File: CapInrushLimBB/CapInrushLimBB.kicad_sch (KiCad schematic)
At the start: 31 parts, among them J1 Screw_Terminal_01x02, J2 Screw_Terminal_01x02, K1 G5LE-1A, Q1 MPSA42, Q2 IRF9540N, Q3 TIP41C, Q4 BSP230 300V 0.21A, U1 LM385Z-ADJ

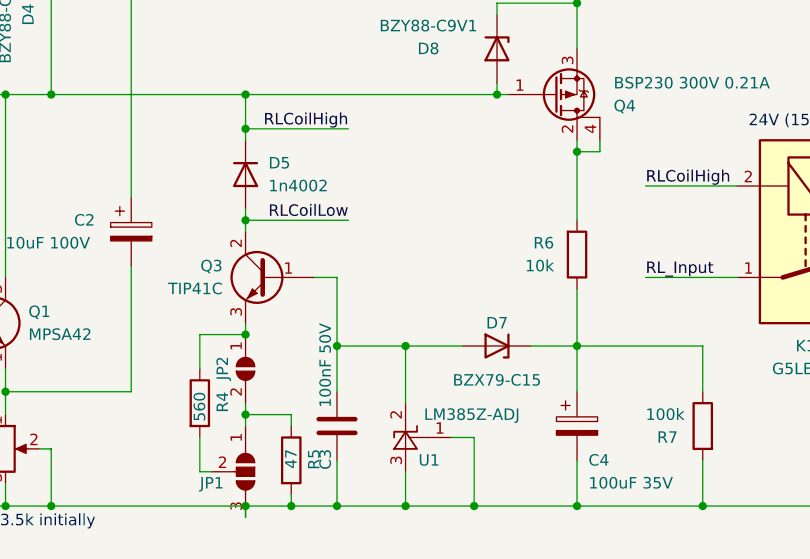
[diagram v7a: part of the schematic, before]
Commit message: Updating model, schematic and PCB to remove cap. on the relay timer ref. and to fit a zener across the relay coil.
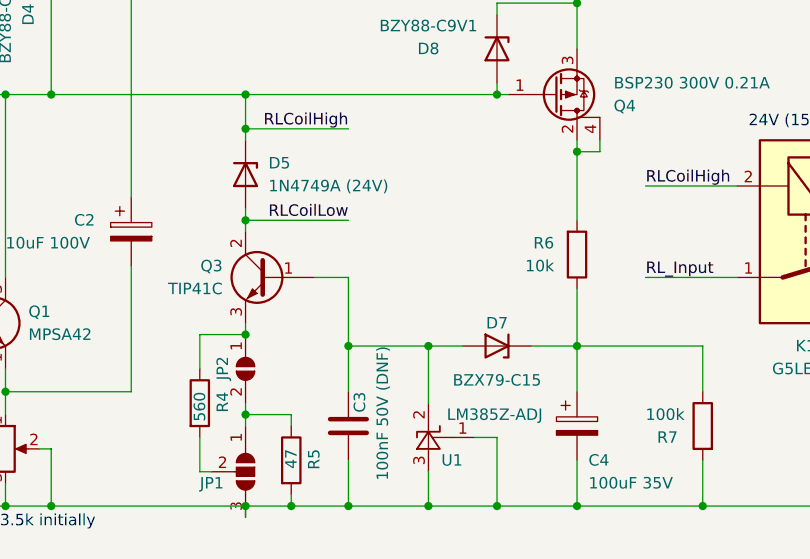
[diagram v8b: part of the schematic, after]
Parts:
- removed D5: 1n4002, Diode_THT:D_DO-41_SOD81_P2.54mm_Vertical_KathodeUp, symbol Device:D
- added D5: 1N4749A (24V), Diode_THT:D_DO-41_SOD81_P2.54mm_Vertical_KathodeUp, symbol Device:D_Zener
- C3: value 100nF 50V -> 100nF 50V (DNF)
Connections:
- net RLCoilHigh: now also D5.1 (K)
- net RLCoilLow: now also D5.2 (A)
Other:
- moved on the sheet: C3, U1
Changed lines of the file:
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@@
   (junction (at 196.85 116.84) (diameter 0) (color 0 0 0 0)
   )
-  (junction (at 142.24 139.7) (diameter 0) (color 0 0 0 0)
-  )
   (junction (at 124.46 97.79) (diameter 0) (color 0 0 0 0)
   )
   (junction (at 102.87 139.7) (diameter 0) (color 0 0 0 0)
   )
+  (junction (at 135.89 139.7) (diameter 0) (color 0 0 0 0)
+  )
   (junction (at 97.79 139.7) (diameter 0) (color 0 0 0 0)
   )
@@
   (junction (at 68.58 139.7) (diameter 0) (color 0 0 0 0)
   )
-  (junction (at 142.24 121.92) (diameter 0) (color 0 0 0 0)
-  )
   (junction (at 124.46 120.65) (diameter 0) (color 0 0 0 0)
   )
@@
   (junction (at 124.46 129.54) (diameter 0) (color 0 0 0 0)
   )
-  (junction (at 134.62 139.7) (diameter 0) (color 0 0 0 0)
-  )
-  (junction (at 149.86 139.7) (diameter 0) (color 0 0 0 0)
+  (junction (at 135.89 121.92) (diameter 0) (color 0 0 0 0)
+  )
+  (junction (at 144.78 139.7) (diameter 0) (color 0 0 0 0)
   )
   (junction (at 111.76 73.66) (diameter 0) (color 0 0 0 0)
   )
+  (junction (at 152.4 139.7) (diameter 0) (color 0 0 0 0)
+  )
   (junction (at 175.26 139.7) (diameter 0) (color 0 0 0 0)
   )
+  (junction (at 144.78 121.92) (diameter 0) (color 0 0 0 0)
+  )
   (junction (at 129.54 139.7) (diameter 0) (color 0 0 0 0)
   )
@@
   (junction (at 97.79 93.98) (diameter 0) (color 0 0 0 0)
   )
-  (junction (at 134.62 121.92) (diameter 0) (color 0 0 0 0)
-  )
   (junction (at 93.98 73.66) (diameter 0) (color 0 0 0 0)
   )
@@
     (stroke (width 0) (type default) (color 0 0 0 0))
   )
-  (wire (pts (xy 149.86 139.7) (xy 161.29 139.7))
+  (wire (pts (xy 144.78 139.7) (xy 152.4 139.7))
     (stroke (width 0) (type default) (color 0 0 0 0))
   )
@@
     (stroke (width 0) (type default) (color 0 0 0 0))
   )
-  (wire (pts (xy 132.08 114.3) (xy 134.62 114.3))
+  (wire (pts (xy 132.08 114.3) (xy 135.89 114.3))
     (stroke (width 0) (type default) (color 0 0 0 0))
   )
@@
     (stroke (width 0) (type default) (color 0 0 0 0))
   )
-  (wire (pts (xy 149.86 132.08) (xy 149.86 139.7))
+  (wire (pts (xy 152.4 132.08) (xy 152.4 139.7))
     (stroke (width 0) (type default) (color 0 0 0 0))
   )
@@
     (stroke (width 0) (type default) (color 0 0 0 0))
   )
-  (wire (pts (xy 134.62 139.7) (xy 142.24 139.7))
-    (stroke (width 0) (type default) (color 0 0 0 0))
-  )
-  (wire (pts (xy 142.24 121.92) (xy 148.59 121.92))
-    (stroke (width 0) (type default) (color 0 0 0 0))
-  )
   (wire (pts (xy 194.31 116.84) (xy 196.85 116.84))
     (stroke (width 0) (type default) (color 0 0 0 0))
@@
     (stroke (width 0) (type default) (color 0 0 0 0))
   )
+  (wire (pts (xy 135.89 139.7) (xy 144.78 139.7))
+    (stroke (width 0) (type default) (color 0 0 0 0))
+  )
   (wire (pts (xy 119.38 120.65) (xy 119.38 124.46))
     (stroke (width 0) (type default) (color 0 0 0 0))
@@
     (stroke (width 0) (type default) (color 0 0 0 0))
   )
-  (wire (pts (xy 134.62 114.3) (xy 134.62 121.92))
+  (wire (pts (xy 135.89 114.3) (xy 135.89 121.92))
     (stroke (width 0) (type default) (color 0 0 0 0))
   )
@@
     (stroke (width 0) (type default) (color 0 0 0 0))
   )
-  (wire (pts (xy 134.62 121.92) (xy 142.24 121.92))
-    (stroke (width 0) (type default) (color 0 0 0 0))
-  )
   (wire (pts (xy 175.26 139.7) (xy 199.39 139.7))
     (stroke (width 0) (type default) (color 0 0 0 0))
@@
     (stroke (width 0) (type default) (color 0 0 0 0))
   )
-  (wire (pts (xy 142.24 139.7) (xy 149.86 139.7))
-    (stroke (width 0) (type default) (color 0 0 0 0))
-  )
   (wire (pts (xy 68.58 111.76) (xy 68.58 119.38))
     (stroke (width 0) (type default) (color 0 0 0 0))
@@
     (stroke (width 0) (type default) (color 0 0 0 0))
   )
-  (wire (pts (xy 147.32 132.08) (xy 149.86 132.08))
+  (wire (pts (xy 149.86 132.08) (xy 152.4 132.08))
     (stroke (width 0) (type default) (color 0 0 0 0))
   )
@@
     (stroke (width 0) (type default) (color 0 0 0 0))
   )
+  (wire (pts (xy 144.78 121.92) (xy 148.59 121.92))
+    (stroke (width 0) (type default) (color 0 0 0 0))
+  )
   (wire (pts (xy 124.46 107.95) (xy 135.89 107.95))
     (stroke (width 0) (type default) (color 0 0 0 0))
@@
     (stroke (width 0) (type default) (color 0 0 0 0))
   )
-  (wire (pts (xy 142.24 121.92) (xy 142.24 128.27))
+  (wire (pts (xy 152.4 139.7) (xy 161.29 139.7))
+    (stroke (width 0) (type default) (color 0 0 0 0))
+  )
+  (wire (pts (xy 144.78 121.92) (xy 144.78 128.27))
     (stroke (width 0) (type default) (color 0 0 0 0))
   )
@@
     (stroke (width 0) (type default) (color 0 0 0 0))
   )
-  (wire (pts (xy 142.24 135.89) (xy 142.24 139.7))
+  (wire (pts (xy 144.78 135.89) (xy 144.78 139.7))
     (stroke (width 0) (type default) (color 0 0 0 0))
   )
@@
     (stroke (width 0) (type default) (color 0 0 0 0))
   )
+  (wire (pts (xy 135.89 121.92) (xy 144.78 121.92))
+    (stroke (width 0) (type default) (color 0 0 0 0))
+  )
   (wire (pts (xy 52.07 71.12) (xy 52.07 73.66))
     (stroke (width 0) (type default) (color 0 0 0 0))
@@
     (stroke (width 0) (type default) (color 0 0 0 0))
   )
-  (wire (pts (xy 134.62 134.62) (xy 134.62 139.7))
+  (wire (pts (xy 135.89 134.62) (xy 135.89 139.7))
     (stroke (width 0) (type default) (color 0 0 0 0))
   )
@@
     (stroke (width 0) (type default) (color 0 0 0 0))
   )
-  (wire (pts (xy 129.54 139.7) (xy 134.62 139.7))
-    (stroke (width 0) (type default) (color 0 0 0 0))
-  )
-  (wire (pts (xy 134.62 121.92) (xy 134.62 127))
+  (wire (pts (xy 129.54 139.7) (xy 135.89 139.7))
+    (stroke (width 0) (type default) (color 0 0 0 0))
+  )
+  (wire (pts (xy 135.89 121.92) (xy 135.89 127))
     (stroke (width 0) (type default) (color 0 0 0 0))
   )
@@
     (pin "2")
   )
-  (symbol (lib_id "Device:D") (at 124.46 102.87 270) (unit 1)
+  (symbol (lib_id "Device:D_Zener") (at 124.46 102.87 270) (unit 1)
     (in_bom yes) (on_board yes) (fields_autoplaced)
     (property "Reference" "D5" (id 0) (at 127 101.5999 90)
       (effects (font (size 1.27 1.27)) (justify left))
     )
-    (property "Value" "1n4002" (id 1) (at 127 104.1399 90)
+    (property "Value" "1N4749A (24V)" (id 1) (at 127 104.1399 90)
       (effects (font (size 1.27 1.27)) (justify left))
     )
@@
     (pin "2")
   )
-  (symbol (lib_id "Device:C") (at 134.62 130.81 180) (unit 1)
-    (in_bom yes) (on_board yes)
-    (property "Reference" "C3" (id 0) (at 133.35 133.35 90)
-      (effects (font (size 1.27 1.27)) (justify left))
-    )
-    (property "Value" "100nF 50V" (id 1) (at 133.35 119.38 90)
-      (effects (font (size 1.27 1.27)) (justify left))
-    )
-    (property "Footprint" "Capacitor_THT:C_Disc_D5.1mm_W3.2mm_P5.00mm" (id 2) (at 133.6548 127 0)
-      (effects (font (size 1.27 1.27)) hide)
-    )
-    (property "Datasheet" "~" (id 3) (at 134.62 130.81 0)
-      (effects (font (size 1.27 1.27)) hide)
-    )
-    (pin "1")
-    (pin "2")
-  )
-  (symbol (lib_id "Reference_Voltage:LM385Z-ADJ") (at 142.24 132.08 270) (mirror x) (unit 1)
-    (in_bom yes) (on_board yes)
-    (property "Reference" "U1" (id 0) (at 146.05 134.62 90)
-      (effects (font (size 1.27 1.27)) (justify right))
-    )
-    (property "Value" "LM385Z-ADJ" (id 1) (at 154.94 129.54 90)
-      (effects (font (size 1.27 1.27)) (justify right))
-    )
-    (property "Footprint" "CapInrushLim:TO-92_Inline" (id 2) (at 137.16 132.08 0)
+  (symbol (lib_id "Device:C") (at 135.89 130.81 180) (unit 1)
+    (in_bom yes) (on_board yes)
+    (property "Reference" "C3" (id 0) (at 137.16 127 90)
+      (effects (font (size 1.27 1.27)) (justify left))
+    )
+    (property "Value" "100nF 50V (DNF)" (id 1) (at 139.7 121.92 90)
+      (effects (font (size 1.27 1.27)) (justify left))
+    )
+    (property "Footprint" "Capacitor_THT:C_Disc_D5.1mm_W3.2mm_P5.00mm" (id 2) (at 134.9248 127 0)
+      (effects (font (size 1.27 1.27)) hide)
+    )
+    (property "Datasheet" "~" (id 3) (at 135.89 130.81 0)
+      (effects (font (size 1.27 1.27)) hide)
+    )
+    (pin "1")
+    (pin "2")
+  )
+  (symbol (lib_id "Reference_Voltage:LM385Z-ADJ") (at 144.78 132.08 270) (mirror x) (unit 1)
+    (in_bom yes) (on_board yes)
+    (property "Reference" "U1" (id 0) (at 148.59 134.62 90)
+      (effects (font (size 1.27 1.27)) (justify right))
+    )
+    (property "Value" "LM385Z-ADJ" (id 1) (at 157.48 129.54 90)
+      (effects (font (size 1.27 1.27)) (justify right))
+    )
+    (property "Footprint" "CapInrushLim:TO-92_Inline" (id 2) (at 139.7 132.08 0)
       (effects (font (size 1.27 1.27) italic) hide)
     )
-    (property "Datasheet" "http://www.ti.com/lit/ds/symlink/lm185-adj.pdf" (id 3) (at 142.24 132.08 0)
+    (property "Datasheet" "http://www.ti.com/lit/ds/symlink/lm185-adj.pdf" (id 3) (at 144.78 132.08 0)
       (effects (font (size 1.27 1.27) italic) hide)
     )
@@
     )
     (path "/c42c87d9-6630-4bdd-b504-0fc4fcaddf1b"
-      (reference "C3") (unit 1) (value "100nF 50V") (footprint "Capacitor_THT:C_Disc_D5.1mm_W3.2mm_P5.00mm")
+      (reference "C3") (unit 1) (value "100nF 50V (DNF)") (footprint "Capacitor_THT:C_Disc_D5.1mm_W3.2mm_P5.00mm")
     )
     (path "/d60a5db2-8cd8-4af1-8cbf-01714930ea15"
@@
       (reference "D4") (unit 1) (value "BZY88-C9V1") (footprint "Diode_THT:D_DO-35_SOD27_P3.81mm_Vertical_AnodeUp")
     )
-    (path "/b236afa7-5ddc-4fa0-8b38-6e2f2c55b1a6"
-      (reference "D5") (unit 1) (value "1n4002") (footprint "Diode_THT:D_DO-41_SOD81_P2.54mm_Vertical_KathodeUp")
+    (path "/aaf70202-fa2c-4218-9bfa-a88dd718e9bd"
+      (reference "D5") (unit 1) (value "1N4749A (24V)") (footprint "Diode_THT:D_DO-41_SOD81_P2.54mm_Vertical_KathodeUp")
     )
     (path "/8b036306-9b43-4d58-90a3-f75924c14fc9"
